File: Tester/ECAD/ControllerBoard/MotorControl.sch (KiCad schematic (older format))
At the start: 12 parts, among them U3 DRV8833PW, U4 DRV8833PW

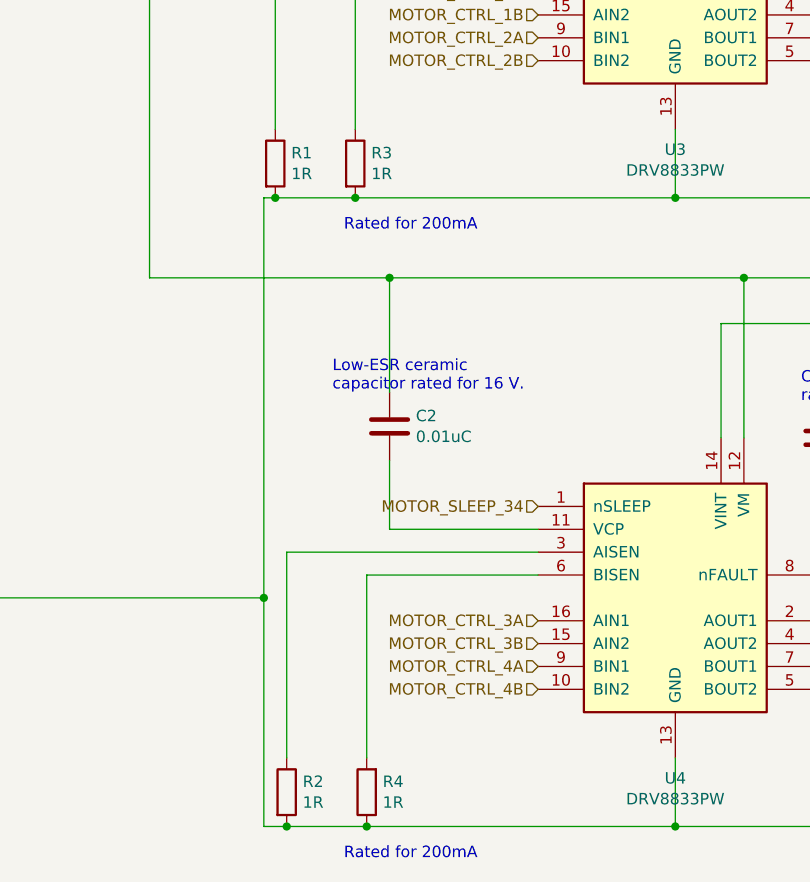
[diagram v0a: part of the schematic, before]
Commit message: Progressed circuit layout.
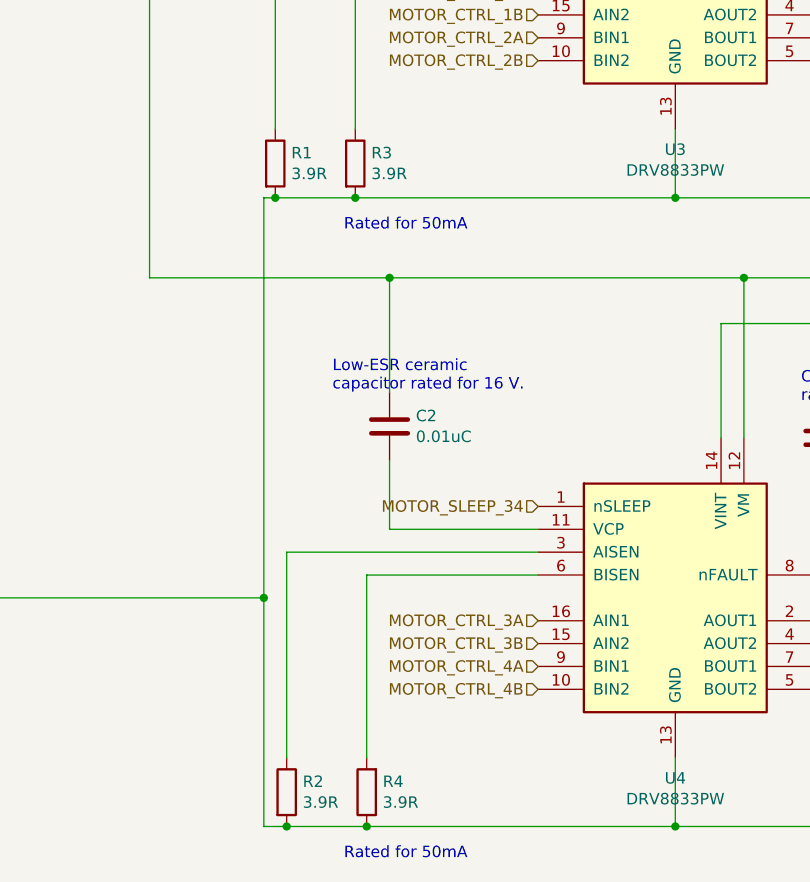
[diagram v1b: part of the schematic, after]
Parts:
- R1, R2, R3, R4: value 1R -> 3.9R; footprint Resistor_SMD:R_0805_2012Metric_Pad1.15x1.40mm_HandSolder -> Resistor_SMD:R_1206_3216Metric_Pad1.42x1.75mm_HandSolder; Manufacturer Part Number RC0805FR-071RL -> CRCW12063R90FKEA
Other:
- note added: "Rated for 50mA"
- note removed: "Rated for 200mA"
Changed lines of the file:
@@
 $Descr A4 11693 8268
 encoding utf-8
-Sheet 2 5
+Sheet 2 6
 Title ""
 Date ""
@@
 P 4500 5900
 F 0 "R4" H 4430 5854 50  0000 R CNN
-F 1 "1R" H 4430 5945 50  0000 R CNN
-F 2 "Resistor_SMD:R_0805_2012Metric_Pad1.15x1.40mm_HandSolder" V 4430 5900 50  0001 C CNN
+F 1 "3.9R" H 4430 5945 50  0000 R CNN
+F 2 "Resistor_SMD:R_1206_3216Metric_Pad1.42x1.75mm_HandSolder" V 4430 5900 50  0001 C CNN
 F 3 "~" H 4500 5900 50  0001 C CNN
-F 4 "RC0805FR-071RL" H 4500 5900 50  0001 C CNN "Manufacturer Part Number"
+F 4 "CRCW12063R90FKEA" H 4500 5900 50  0001 C CNN "Manufacturer Part Number"
 	1    4500 5900
 	-1   0    0    1
@@
 P 4150 5900
 F 0 "R2" H 4220 5946 50  0000 L CNN
-F 1 "1R" H 4220 5855 50  0000 L CNN
-F 2 "Resistor_SMD:R_0805_2012Metric_Pad1.15x1.40mm_HandSolder" V 4080 5900 50  0001 C CNN
+F 1 "3.9R" H 4220 5855 50  0000 L CNN
+F 2 "Resistor_SMD:R_1206_3216Metric_Pad1.42x1.75mm_HandSolder" V 4080 5900 50  0001 C CNN
 F 3 "~" H 4150 5900 50  0001 C CNN
-F 4 "RC0805FR-071RL" H 4150 5900 50  0001 C CNN "Manufacturer Part Number"
+F 4 "CRCW12063R90FKEA" H 4150 5900 50  0001 C CNN "Manufacturer Part Number"
 	1    4150 5900
 	1    0    0    -1
@@
 P 4450 3150
 F 0 "R3" H 4520 3196 50  0000 L CNN
-F 1 "1R" H 4520 3105 50  0000 L CNN
-F 2 "Resistor_SMD:R_0805_2012Metric_Pad1.15x1.40mm_HandSolder" V 4380 3150 50  0001 C CNN
+F 1 "3.9R" H 4520 3105 50  0000 L CNN
+F 2 "Resistor_SMD:R_1206_3216Metric_Pad1.42x1.75mm_HandSolder" V 4380 3150 50  0001 C CNN
 F 3 "~" H 4450 3150 50  0001 C CNN
-F 4 "RC0805FR-071RL" H 4450 3150 50  0001 C CNN "Manufacturer Part Number"
+F 4 "CRCW12063R90FKEA" H 4450 3150 50  0001 C CNN "Manufacturer Part Number"
 	1    4450 3150
 	1    0    0    -1
@@
 P 4100 3150
 F 0 "R1" H 4170 3196 50  0000 L CNN
-F 1 "1R" H 4170 3105 50  0000 L CNN
-F 2 "Resistor_SMD:R_0805_2012Metric_Pad1.15x1.40mm_HandSolder" V 4030 3150 50  0001 C CNN
+F 1 "3.9R" H 4170 3105 50  0000 L CNN
+F 2 "Resistor_SMD:R_1206_3216Metric_Pad1.42x1.75mm_HandSolder" V 4030 3150 50  0001 C CNN
 F 3 "~" H 4100 3150 50  0001 C CNN
-F 4 "RC0805FR-071RL" H 4100 3150 50  0001 C CNN "Manufacturer Part Number"
+F 4 "CRCW12063R90FKEA" H 4100 3150 50  0001 C CNN "Manufacturer Part Number"
 	1    4100 3150
 	1    0    0    -1
@@
 	4100 3000 4100 2100
 Text Notes 4400 3450 0    50   ~ 0
-Rated for 200mA
+Rated for 50mA
 Text Notes 4400 6200 0    50   ~ 0
-Rated for 200mA
+Rated for 50mA
 Text HLabel 5250 2400 0    50   Input ~ 0
 MOTOR_CTRL_1A

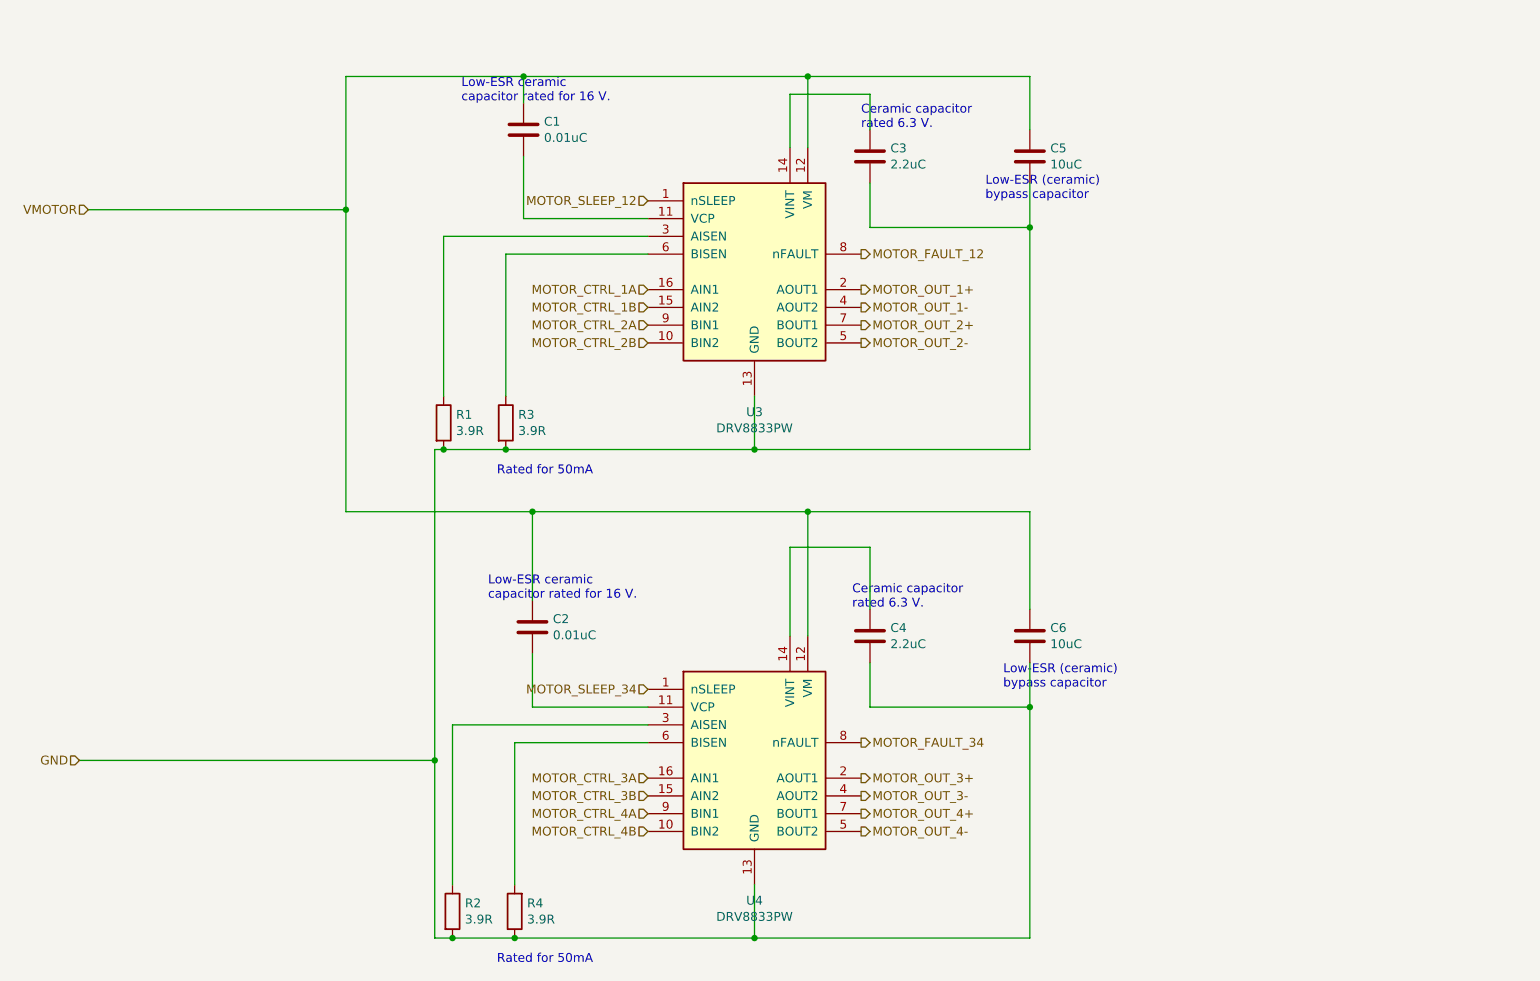
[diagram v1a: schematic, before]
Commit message: Progressed circuit layout.
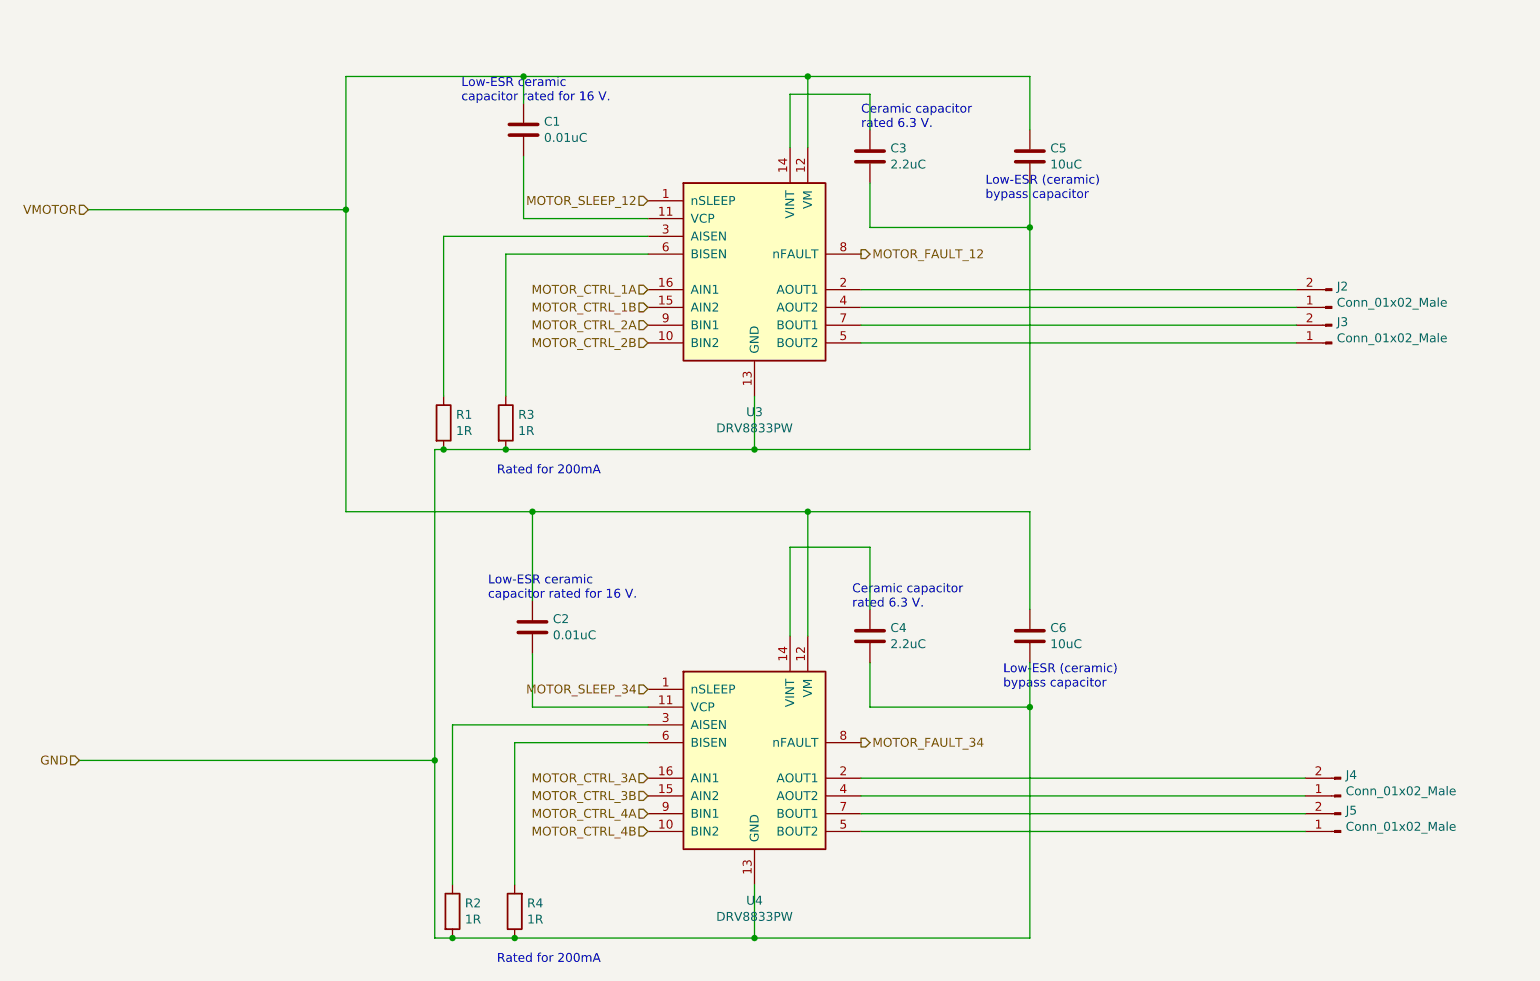
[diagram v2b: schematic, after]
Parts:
- added J2, J3, J4, J5: Conn_01x02_Male, Connector_Molex:Molex_PicoBlade_53048-0210_1x02_P1.25mm_Horizontal, symbol Connector:Conn_01x02_Male
- R1, R2, R3, R4: value 3.9R -> 1R; footprint Resistor_SMD:R_1206_3216Metric_Pad1.42x1.75mm_HandSolder -> Resistor_SMD:R_0805_2012Metric_Pad1.15x1.40mm_HandSolder; Manufacturer Part Number CRCW12063R90FKEA -> RC0805FR-071RL
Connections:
- net MOTOR_OUT_1+: no longer names the net of U3.2 (AOUT1)
- net MOTOR_OUT_1+: now also J2.2 (Pin_2)
- net MOTOR_OUT_1-: no longer names the net of U3.4 (AOUT2)
- net MOTOR_OUT_1-: now also J2.1 (Pin_1)
- net MOTOR_OUT_2+: no longer names the net of U3.7 (BOUT1)
- net MOTOR_OUT_2+: now also J3.2 (Pin_2)
- net MOTOR_OUT_2-: no longer names the net of U3.5 (BOUT2)
- net MOTOR_OUT_2-: now also J3.1 (Pin_1)
- net MOTOR_OUT_3+: no longer names the net of U4.2 (AOUT1)
- net MOTOR_OUT_3+: now also J4.2 (Pin_2)
- net MOTOR_OUT_3-: no longer names the net of U4.4 (AOUT2)
- net MOTOR_OUT_3-: now also J4.1 (Pin_1)
- net MOTOR_OUT_4+: no longer names the net of U4.7 (BOUT1)
- net MOTOR_OUT_4+: now also J5.2 (Pin_2)
- net MOTOR_OUT_4-: no longer names the net of U4.5 (BOUT2)
- net MOTOR_OUT_4-: now also J5.1 (Pin_1)
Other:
- note added: "Rated for 200mA"
- note removed: "Rated for 50mA"
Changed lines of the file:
@@
 Comment4 ""
 $EndDescr
-Text HLabel 6450 2700 2    50   Output ~ 0
-MOTOR_OUT_2-
-Text HLabel 6450 2600 2    50   Output ~ 0
-MOTOR_OUT_2+
-Text HLabel 6450 2500 2    50   Output ~ 0
-MOTOR_OUT_1-
-Text HLabel 6450 2400 2    50   Output ~ 0
-MOTOR_OUT_1+
-Text HLabel 6450 5450 2    50   Output ~ 0
-MOTOR_OUT_4-
-Text HLabel 6450 5350 2    50   Output ~ 0
-MOTOR_OUT_4+
-Text HLabel 6450 5250 2    50   Output ~ 0
-MOTOR_OUT_3-
-Text HLabel 6450 5150 2    50   Output ~ 0
-MOTOR_OUT_3+
 $Comp
 L Device:R R4
@@
 P 4500 5900
 F 0 "R4" H 4430 5854 50  0000 R CNN
-F 1 "3.9R" H 4430 5945 50  0000 R CNN
-F 2 "Resistor_SMD:R_1206_3216Metric_Pad1.42x1.75mm_HandSolder" V 4430 5900 50  0001 C CNN
+F 1 "1R" H 4430 5945 50  0000 R CNN
+F 2 "Resistor_SMD:R_0805_2012Metric_Pad1.15x1.40mm_HandSolder" V 4430 5900 50  0001 C CNN
 F 3 "~" H 4500 5900 50  0001 C CNN
-F 4 "CRCW12063R90FKEA" H 4500 5900 50  0001 C CNN "Manufacturer Part Number"
+F 4 "RC0805FR-071RL" H 4500 5900 50  0001 C CNN "Manufacturer Part Number"
 	1    4500 5900
 	-1   0    0    1
@@
 P 4150 5900
 F 0 "R2" H 4220 5946 50  0000 L CNN
-F 1 "3.9R" H 4220 5855 50  0000 L CNN
-F 2 "Resistor_SMD:R_1206_3216Metric_Pad1.42x1.75mm_HandSolder" V 4080 5900 50  0001 C CNN
+F 1 "1R" H 4220 5855 50  0000 L CNN
+F 2 "Resistor_SMD:R_0805_2012Metric_Pad1.15x1.40mm_HandSolder" V 4080 5900 50  0001 C CNN
 F 3 "~" H 4150 5900 50  0001 C CNN
-F 4 "CRCW12063R90FKEA" H 4150 5900 50  0001 C CNN "Manufacturer Part Number"
+F 4 "RC0805FR-071RL" H 4150 5900 50  0001 C CNN "Manufacturer Part Number"
 	1    4150 5900
 	1    0    0    -1
@@
 P 4450 3150
 F 0 "R3" H 4520 3196 50  0000 L CNN
-F 1 "3.9R" H 4520 3105 50  0000 L CNN
-F 2 "Resistor_SMD:R_1206_3216Metric_Pad1.42x1.75mm_HandSolder" V 4380 3150 50  0001 C CNN
+F 1 "1R" H 4520 3105 50  0000 L CNN
+F 2 "Resistor_SMD:R_0805_2012Metric_Pad1.15x1.40mm_HandSolder" V 4380 3150 50  0001 C CNN
 F 3 "~" H 4450 3150 50  0001 C CNN
-F 4 "CRCW12063R90FKEA" H 4450 3150 50  0001 C CNN "Manufacturer Part Number"
+F 4 "RC0805FR-071RL" H 4450 3150 50  0001 C CNN "Manufacturer Part Number"
 	1    4450 3150
 	1    0    0    -1
@@
 P 4100 3150
 F 0 "R1" H 4170 3196 50  0000 L CNN
-F 1 "3.9R" H 4170 3105 50  0000 L CNN
-F 2 "Resistor_SMD:R_1206_3216Metric_Pad1.42x1.75mm_HandSolder" V 4030 3150 50  0001 C CNN
+F 1 "1R" H 4170 3105 50  0000 L CNN
+F 2 "Resistor_SMD:R_0805_2012Metric_Pad1.15x1.40mm_HandSolder" V 4030 3150 50  0001 C CNN
 F 3 "~" H 4100 3150 50  0001 C CNN
-F 4 "CRCW12063R90FKEA" H 4100 3150 50  0001 C CNN "Manufacturer Part Number"
+F 4 "RC0805FR-071RL" H 4100 3150 50  0001 C CNN "Manufacturer Part Number"
 	1    4100 3150
 	1    0    0    -1
@@
 	4100 3000 4100 2100
 Text Notes 4400 3450 0    50   ~ 0
-Rated for 50mA
+Rated for 200mA
 Text Notes 4400 6200 0    50   ~ 0
-Rated for 50mA
+Rated for 200mA
 Text HLabel 5250 2400 0    50   Input ~ 0
 MOTOR_CTRL_1A
@@
 Wire Wire Line
 	4050 5050 4050 6050
+$Comp
+L Connector:Conn_01x02_Male J2
+U 1 1 5E623A42
+P 9100 2500
+AR Path="/5E507163/5E623A42" Ref="J2"  Part="1"
+AR Path="/5E623A42" Ref="J?"  Part="1"
+F 0 "J2" H 9072 2382 50  0000 R CNN
+F 1 "Conn_01x02_Male" H 9072 2473 50  0000 R CNN
+F 2 "Connector_Molex:Molex_PicoBlade_53048-0210_1x02_P1.25mm_Horizontal" H 9100 2500 50  0001 C CNN
+F 3 "~" H 9100 2500 50  0001 C CNN
+F 4 "0530480210" H 9100 2500 50  0001 C CNN "Manufacturer Part Number"
+	1    9100 2500
+	-1   0    0    1
+$EndComp
+$Comp
+L Connector:Conn_01x02_Male J3
+U 1 1 5E623A49
+P 9100 2700
+AR Path="/5E507163/5E623A49" Ref="J3"  Part="1"
+AR Path="/5E623A49" Ref="J?"  Part="1"
+F 0 "J3" H 9072 2582 50  0000 R CNN
+F 1 "Conn_01x02_Male" H 9072 2673 50  0000 R CNN
+F 2 "Connector_Molex:Molex_PicoBlade_53048-0210_1x02_P1.25mm_Horizontal" H 9100 2700 50  0001 C CNN
+F 3 "~" H 9100 2700 50  0001 C CNN
+F 4 "0530480210" H 9100 2700 50  0001 C CNN "Manufacturer Part Number"
+	1    9100 2700
+	-1   0    0    1
+$EndComp
+$Comp
+L Connector:Conn_01x02_Male J4
+U 1 1 5E623A50
+P 9150 5250
+AR Path="/5E507163/5E623A50" Ref="J4"  Part="1"
+AR Path="/5E623A50" Ref="J?"  Part="1"
+F 0 "J4" H 9122 5132 50  0000 R CNN
+F 1 "Conn_01x02_Male" H 9122 5223 50  0000 R CNN
+F 2 "Connector_Molex:Molex_PicoBlade_53048-0210_1x02_P1.25mm_Horizontal" H 9150 5250 50  0001 C CNN
+F 3 "~" H 9150 5250 50  0001 C CNN
+F 4 "0530480210" H 9150 5250 50  0001 C CNN "Manufacturer Part Number"
+	1    9150 5250
+	-1   0    0    1
+$EndComp
+$Comp
+L Connector:Conn_01x02_Male J5
+U 1 1 5E623A57
+P 9150 5450
+AR Path="/5E507163/5E623A57" Ref="J5"  Part="1"
+AR Path="/5E623A57" Ref="J?"  Part="1"
+F 0 "J5" H 9122 5332 50  0000 R CNN
+F 1 "Conn_01x02_Male" H 9122 5423 50  0000 R CNN
+F 2 "Connector_Molex:Molex_PicoBlade_53048-0210_1x02_P1.25mm_Horizontal" H 9150 5450 50  0001 C CNN
+F 3 "~" H 9150 5450 50  0001 C CNN
+F 4 "0530480210" H 9150 5450 50  0001 C CNN "Manufacturer Part Number"
+	1    9150 5450
+	-1   0    0    1
+$EndComp
+Wire Wire Line
+	6450 2400 8900 2400
+Wire Wire Line
+	6450 2500 8900 2500
+Wire Wire Line
+	6450 2600 8900 2600
+Wire Wire Line
+	6450 2700 8900 2700
+Wire Wire Line
+	6450 5150 8950 5150
+Wire Wire Line
+	8950 5250 6450 5250
+Wire Wire Line
+	6450 5350 8950 5350
+Wire Wire Line
+	8950 5450 6450 5450
 $EndSCHEMATC
